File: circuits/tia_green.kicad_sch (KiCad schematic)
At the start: 11 parts, among them U3 OPA380AID

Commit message: Checkpoint laser controller fab parity package
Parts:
- removed C9: 10pF C0G, Capacitor_SMD:C_0603_1608Metric_Pad1.08x0.95mm_HandSolder, symbol viv:C_H
- removed R12: 10k, Resistor_SMD:R_0603_1608Metric_Pad0.98x0.95mm_HandSolder, symbol viv:R_V
- removed RV7: RF 2M, Potentiometer_SMD:Potentiometer_Bourns_3224W_Vertical, symbol viv:POT_H
- added C10: 100nF, Capacitor_SMD:C_0402_1005Metric_Pad0.74x0.62mm_HandSolder, symbol viv:C_V
- added C12: 10uF, Capacitor_SMD:C_0805_2012Metric_Pad1.18x1.45mm_HandSolder, symbol viv:C_V
- added R11: 10k, Resistor_SMD:R_0603_1608Metric_Pad0.98x0.95mm_HandSolder, symbol viv:R_H
- C9: renamed from R11; value 10k -> 10pF C0G; footprint Resistor_SMD:R_0603_1608Metric_Pad0.98x0.95mm_HandSolder -> Capacitor_SMD:C_0603_1608Metric_Pad1.08x0.95mm_HandSolder; symbol viv:R_H -> viv:C_H; LCSC C844918 -> C106245; Part Number CRCW060310K0FKEA -> CC0603JRNPO9BN100
- R12: renamed from C12; value 10uF -> 10k; footprint Capacitor_SMD:C_0805_2012Metric_Pad1.18x1.45mm_HandSolder -> Resistor_SMD:R_0603_1608Metric_Pad0.98x0.95mm_HandSolder; symbol viv:C_V -> viv:R_V; LCSC C318691 -> C844918; Part Number CL21A106KAYNNNG -> CRCW060310K0FKEA
- RV3: renamed from C10; value 100nF -> VBIAS 10k; footprint Capacitor_SMD:C_0402_1005Metric_Pad0.74x0.62mm_HandSolder -> Potentiometer_SMD:Potentiometer_Bourns_3224W_Vertical; symbol viv:C_V -> viv:POT_V; LCSC C83056 -> C81348; Part Number 0402B104K160CT -> 3224W-1-103E
- RV7: renamed from RV3; value VBIAS 10k -> RF 2M; symbol viv:POT_V -> viv:POT_H; LCSC C81348 -> C116323; Part Number 3224W-1-103E -> 3224W-1-205E
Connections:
- net +5V: now also R12.1, C10.1; no longer RV3.1
- net GND: now also RV3.3, C10.2, C12.2; no longer R12.2, RV3.2, RV7.3
- net V_OUT: now also C9.2, RV7.2 (W), RV7.3
- net PD_CATHODE: now reaches C11.1, D3.1 (K), R10.2
- net PD_ANODE: now reaches D3.2 (A), U3.2 (-)
- net PD_ANODE: now also C9.1, RV7.1
- new net VBIAS: C12.1, R11.2, U3.3 (+)
- new net VBIAS_TOP: R12.2, RV3.1
- new net VBIAS_WIPER: R11.1, RV3.2 (W)
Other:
- moved on the sheet: RV7
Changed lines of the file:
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@@
   (no_connect (at 224.79 154.94))
   (no_connect (at 224.79 144.78))
+  (label "PD_ANODE" (at 190.5 130.81 0) (effects (font (size 1.27 1.27)) (justify left bottom)))
+  (label "PD_CATHODE" (at 185.42 130.81 0) (effects (font (size 1.27 1.27)) (justify left bottom)))
+  (label "VBIAS_TOP" (at 165.1 143.51 0) (effects (font (size 1.27 1.27)) (justify left bottom)))
+  (label "VBIAS_WIPER" (at 168.91 152.4 0) (effects (font (size 1.27 1.27)) (justify left bottom)))
+  (label "VBIAS" (at 190.5 152.4 0) (effects (font (size 1.27 1.27)) (justify left bottom)))
   (hierarchical_label "V_OUT" (shape output) (at 232.41 149.86 0) (effects (font (size 1.27 1.27)) (justify left)))
   (text "TIA Channel  —  on-board SFH2201 signal PD → OPA380AID transimpedance amp  ·  reused 4× (IR / RED / GREEN / BLUE)" (at 150 104 0) (effects (font (size 2.0 2.0)) (justify left)))

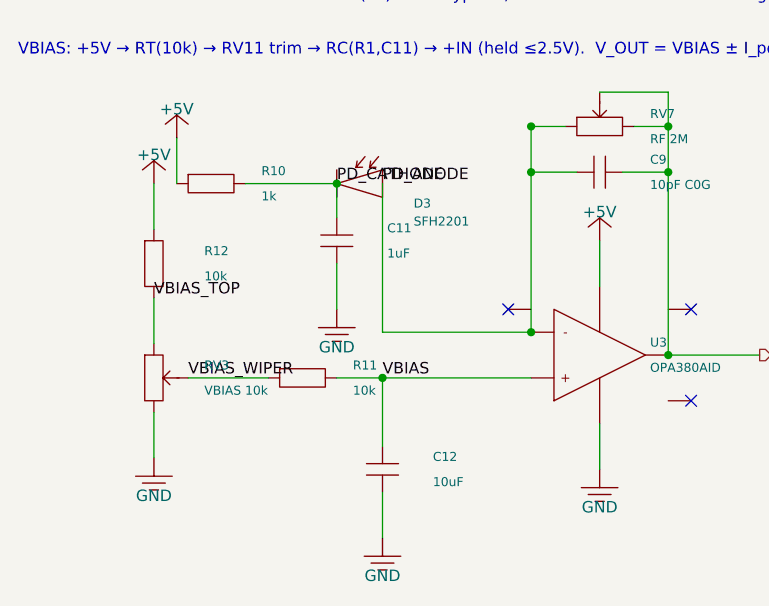
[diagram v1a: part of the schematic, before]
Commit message: Checkpoint schematic warning hygiene
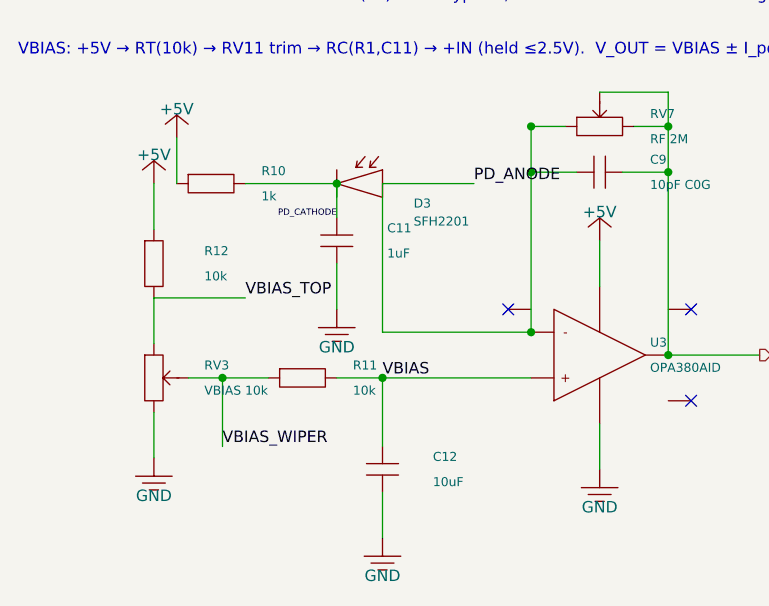
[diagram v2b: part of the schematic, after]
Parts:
- removed C9: 10pF C0G, Capacitor_SMD:C_0603_1608Metric_Pad1.08x0.95mm_HandSolder, symbol viv:C_H
- removed R12: 10k, Resistor_SMD:R_0603_1608Metric_Pad0.98x0.95mm_HandSolder, symbol viv:R_V
- removed RV7: RF 2M, Potentiometer_SMD:Potentiometer_Bourns_3224W_Vertical, symbol viv:POT_H
- added C10: 100nF, Capacitor_SMD:C_0402_1005Metric_Pad0.74x0.62mm_HandSolder, symbol viv:C_V
- added C12: 10uF, Capacitor_SMD:C_0805_2012Metric_Pad1.18x1.45mm_HandSolder, symbol viv:C_V
- added R11: 10k, Resistor_SMD:R_0603_1608Metric_Pad0.98x0.95mm_HandSolder, symbol viv:R_H
- C9: renamed from R11; value 10k -> 10pF C0G; footprint Resistor_SMD:R_0603_1608Metric_Pad0.98x0.95mm_HandSolder -> Capacitor_SMD:C_0603_1608Metric_Pad1.08x0.95mm_HandSolder; symbol viv:R_H -> viv:C_H; LCSC C844918 -> C106245; Part Number CRCW060310K0FKEA -> CC0603JRNPO9BN100
- R12: renamed from C12; value 10uF -> 10k; footprint Capacitor_SMD:C_0805_2012Metric_Pad1.18x1.45mm_HandSolder -> Resistor_SMD:R_0603_1608Metric_Pad0.98x0.95mm_HandSolder; symbol viv:C_V -> viv:R_V; LCSC C318691 -> C844918; Part Number CL21A106KAYNNNG -> CRCW060310K0FKEA
- RV3: renamed from C10; value 100nF -> VBIAS 10k; footprint Capacitor_SMD:C_0402_1005Metric_Pad0.74x0.62mm_HandSolder -> Potentiometer_SMD:Potentiometer_Bourns_3224W_Vertical; symbol viv:C_V -> viv:POT_V; LCSC C83056 -> C81348; Part Number 0402B104K160CT -> 3224W-1-103E
- RV7: renamed from RV3; value VBIAS 10k -> RF 2M; symbol viv:POT_V -> viv:POT_H; LCSC C81348 -> C116323; Part Number 3224W-1-103E -> 3224W-1-205E
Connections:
- net +5V: now also R12.1, C10.1; no longer RV3.1
- net GND: now also RV3.3, C10.2, C12.2; no longer R12.2, RV3.2, RV7.3
- net PD_ANODE: now also C9.1, RV7.1
- net VBIAS: now also C12.1, R11.2; no longer C9.2, R12.1
- net VBIAS_TOP: now also R12.2, RV3.1; no longer RV7.1
- net VBIAS_WIPER: now also RV3.2 (W), R11.1; no longer C9.1, RV7.2 (W)
- net V_OUT: now also C9.2, RV7.2 (W), RV7.3
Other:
- moved on the sheet: RV7
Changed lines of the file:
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@@
   (wire (pts (xy 167.64 130.81) (xy 167.64 125.73)) (stroke (width 0) (type default)))
   (wire (pts (xy 185.42 139.7) (xy 185.42 144.78)) (stroke (width 0) (type default)))
+  (wire (pts (xy 190.5 130.81) (xy 200.66 130.81)) (stroke (width 0) (type default)))
   (wire (pts (xy 207.01 147.32) (xy 207.01 129.54)) (stroke (width 0) (type default)))
   (wire (pts (xy 207.01 129.54) (xy 207.01 124.46)) (stroke (width 0) (type default)))
@@
   (wire (pts (xy 190.5 165.1) (xy 190.5 170.18)) (stroke (width 0) (type default)))
   (wire (pts (xy 165.1 143.51) (xy 165.1 148.59)) (stroke (width 0) (type default)))
-  (wire (pts (xy 168.91 152.4) (xy 177.8 152.4)) (stroke (width 0) (type default)))
+  (wire (pts (xy 168.91 152.4) (xy 172.72 152.4)) (stroke (width 0) (type default)))
+  (wire (pts (xy 172.72 152.4) (xy 177.8 152.4)) (stroke (width 0) (type default)))
   (wire (pts (xy 185.42 152.4) (xy 190.5 152.4)) (stroke (width 0) (type default)))
   (wire (pts (xy 190.5 152.4) (xy 190.5 160.02)) (stroke (width 0) (type default)))
   (wire (pts (xy 190.5 152.4) (xy 207.01 152.4)) (stroke (width 0) (type default)))
+  (wire (pts (xy 165.1 143.51) (xy 175.26 143.51)) (stroke (width 0) (type default)))
+  (wire (pts (xy 172.72 152.4) (xy 172.72 160.02)) (stroke (width 0) (type default)))
   (junction (at 207.01 147.32) (diameter 0) (color 0 0 0 0))
   (junction (at 185.42 130.81) (diameter 0) (color 0 0 0 0))
@@
   (junction (at 222.25 149.86) (diameter 0) (color 0 0 0 0))
   (junction (at 190.5 152.4) (diameter 0) (color 0 0 0 0))
+  (junction (at 172.72 152.4) (diameter 0) (color 0 0 0 0))
   (no_connect (at 204.47 144.78))
   (no_connect (at 224.79 154.94))
   (no_connect (at 224.79 144.78))
-  (label "PD_ANODE" (at 190.5 130.81 0) (effects (font (size 1.27 1.27)) (justify left bottom)))
-  (label "PD_CATHODE" (at 185.42 130.81 0) (effects (font (size 1.27 1.27)) (justify left bottom)))
-  (label "VBIAS_TOP" (at 165.1 143.51 0) (effects (font (size 1.27 1.27)) (justify left bottom)))
-  (label "VBIAS_WIPER" (at 168.91 152.4 0) (effects (font (size 1.27 1.27)) (justify left bottom)))
+  (label "PD_ANODE" (at 200.66 130.81 0) (effects (font (size 1.27 1.27)) (justify left bottom)))
+  (label "PD_CATHODE" (at 185.42 134.62 0) (effects (font (size 0.7 0.7)) (justify right bottom)))
+  (label "VBIAS_TOP" (at 175.26 143.51 0) (effects (font (size 1.27 1.27)) (justify left bottom)))
+  (label "VBIAS_WIPER" (at 172.72 160.02 0) (effects (font (size 1.27 1.27)) (justify left bottom)))
   (label "VBIAS" (at 190.5 152.4 0) (effects (font (size 1.27 1.27)) (justify left bottom)))
   (hierarchical_label "V_OUT" (shape output) (at 232.41 149.86 0) (effects (font (size 1.27 1.27)) (justify left)))
